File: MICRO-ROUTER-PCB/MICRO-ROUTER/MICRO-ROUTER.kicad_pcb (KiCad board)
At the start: 2 copper layers, 85 x 54 mm, 77 parts, among them J2 USB_A, J3 USB_C_Receptacle_USB2.0_16P, J4 Battery Connector, J5 SPI Header, J6 GPIO Header, J7 RJ45 5-2301996-6, Q1 FS8205A, SW2 8Devices Reset, SW3 UART Reset, U1 TP4056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

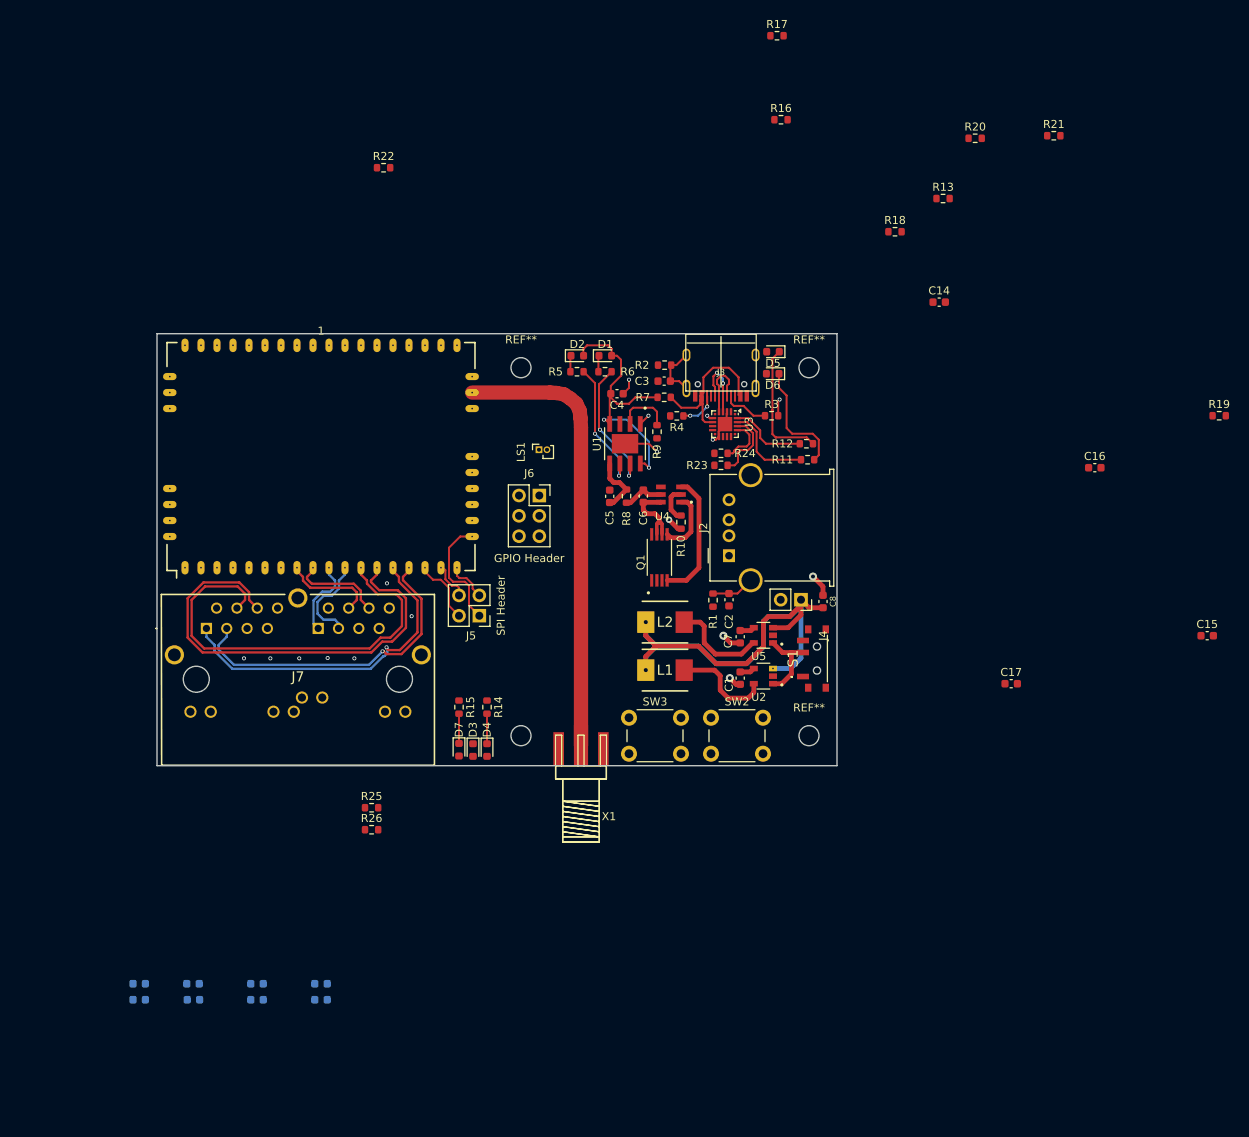
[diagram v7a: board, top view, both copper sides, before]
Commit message: -wired 5v and 3.3v reg -cleaned up remaining footprints
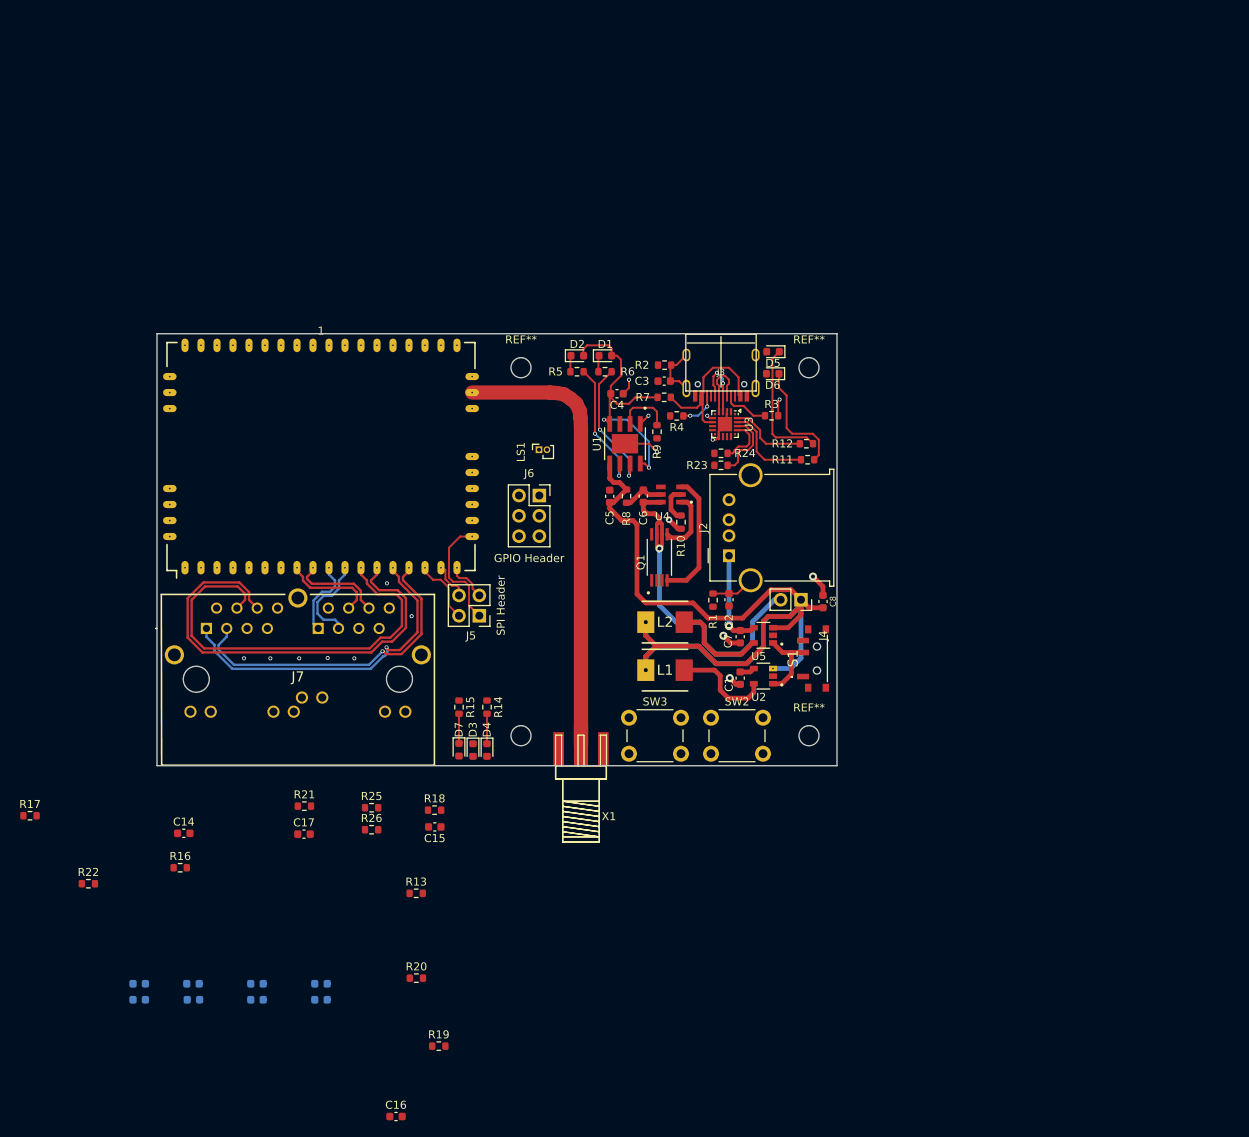
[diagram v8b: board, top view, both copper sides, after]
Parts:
- moved R17 135.0 mm to (34.6, 193.0)
- moved R20 126.1 mm to (82.9, 213.3)
- moved R21 125.7 mm to (68.9, 191.8)
- moved R19 125.4 mm to (85.7, 221.8)
- moved R16 119.9 mm to (53.4, 199.5)
- moved C16 119.2 mm to (80.4, 230.6)
- moved C14 115.4 mm to (53.9, 195.2)
- moved R13 109.0 mm to (82.9, 202.7)
- moved C15 99.5 mm to (85.2, 194.4), turned to 180 degrees
- moved R22 96.8 mm to (41.9, 201.5)
- moved R18 92.4 mm to (85.2, 192.3)
- moved C17 90.4 mm to (68.9, 195.3)
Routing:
- net V-UNREG: track 91.6 -> 129.0 mm
- net Net-(J4-Pin_2): track 9.91 -> 44.2 mm, vias 0 -> 1
- net +5V: track 1.84 -> 12.3 mm, vias 0 -> 1
